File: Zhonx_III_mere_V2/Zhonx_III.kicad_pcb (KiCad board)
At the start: 4 copper layers, 70 x 97 mm, 148 parts, among them K1 L_Motor, K2 R_Motor, K3 USART, P1 JTAG, Q1 BSS138, Q2 BSS138, U1 MCP73213, U10 BSL214N, U11 BSL214N, U12 24LC64T, U14 STM32F405RGT6, U16 Line_1, U17 Line_2, U18 Line_3, U19 Line_4, U2 A3918_L, U20 Line_5, U3 A3918_R, U4 LTC2955CTS8-1, U5 INA219, U6 LT1761-5, U7 LT1761-3.3, U8 LT1761-3.3, U9 LT3684, X1 QUARTZ_8Z

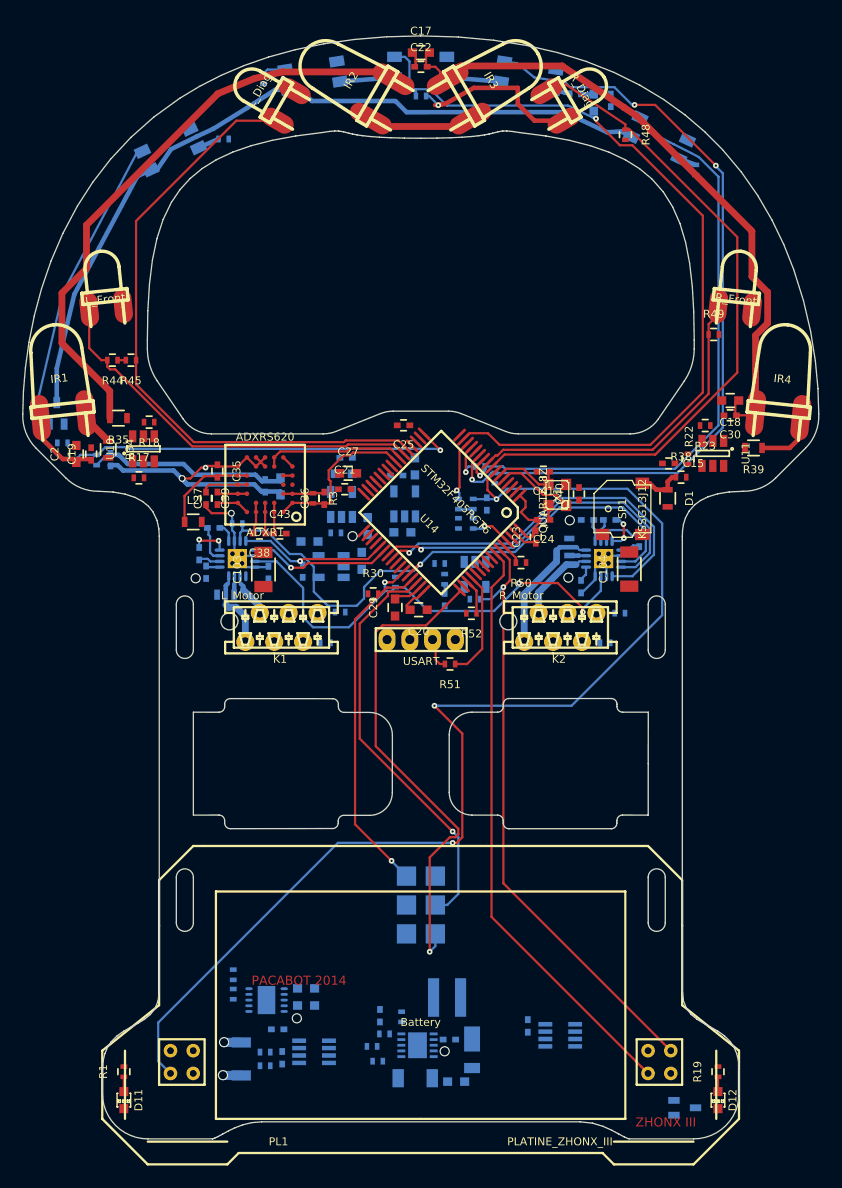
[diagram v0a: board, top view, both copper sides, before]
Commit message: routage pcb (debut ...)
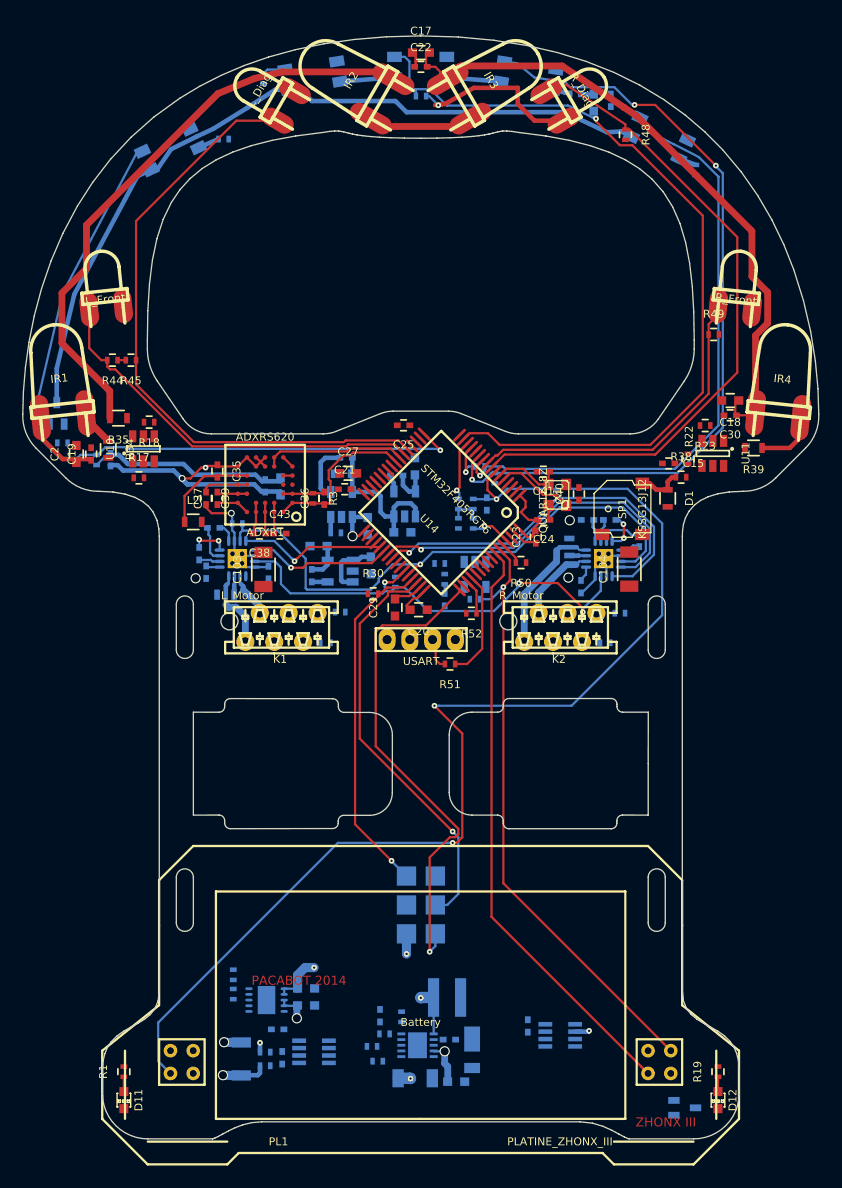
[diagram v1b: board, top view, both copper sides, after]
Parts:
- moved C54 0.89 mm to (98.9, 131.3)
- moved C42 0.89 mm to (103.5, 133.0)
- moved C51 0.89 mm to (98.3, 133.9)
- moved U8 0.89 mm to (100.8, 133.5)
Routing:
- net +4.5V: track 65.1 -> 83.5 mm, vias 0 -> 2
- net +8V: track 159.9 -> 177.8 mm, vias 7 -> 9
- net +9V: track 0.00 -> 15.0 mm, vias 0 -> 2
- net +5V: track 8.52 -> 22.0 mm
- net Net-(C49-Pad1): track 0.00 -> 5.15 mm
- net +3.3V: track 12.7 -> 16.7 mm
- net +3.3VADC: track 39.3 -> 43.0 mm
- net FL: track 44.2 -> 41.1 mm
- net +BATT: track 4.30 -> 6.68 mm
- net Net-(C50-Pad1): track 0.00 -> 1.52 mm
- net Net-(C51-Pad1): track 0.00 -> 1.40 mm
- net EN_PW_ADC: track 0.00 -> 1.40 mm
- net SLEEP: track 51.9 -> 50.6 mm
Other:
- net class Default: clearance 0.15 -> 0.125
- rule trace_clearance: 0.15 -> 0.125
